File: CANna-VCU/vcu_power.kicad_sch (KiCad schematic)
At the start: 21 parts, among them U11 LMR33630CDDA, U12 LD1117S33TR_SOT223

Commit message: first draft of full board
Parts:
- added C21: 10uF, Capacitor_SMD:C_0402_1005Metric, symbol Device:C
- added D2: BZX84Cxx, Package_TO_SOT_SMD:SOT-23, symbol Diode:BZX84Cxx
- added Q1: FDN359BN, Package_TO_SOT_SMD:SOT-23_Handsoldering, symbol SUFST:FDN359BN
- added R9: 100k, Resistor_SMD:R_0402_1005Metric, symbol Device:R
- C20: renamed from C35; footprint Capacitor_SMD:C_0603_1608Metric -> Capacitor_SMD:C_0402_1005Metric
- C22: renamed from C36; footprint Capacitor_SMD:C_0603_1608Metric -> Capacitor_SMD:C_0402_1005Metric
- C23: renamed from C37; footprint Capacitor_SMD:C_0603_1608Metric -> Capacitor_SMD:C_0402_1005Metric
- C24: renamed from C38; footprint Capacitor_SMD:C_0603_1608Metric -> Capacitor_SMD:C_0402_1005Metric
- C25: renamed from C39; footprint Capacitor_SMD:C_0603_1608Metric -> Capacitor_SMD:C_0402_1005Metric
- C26: renamed from C40; footprint Capacitor_SMD:C_0603_1608Metric -> Capacitor_SMD:C_0402_1005Metric
- C27: renamed from C41; footprint Capacitor_SMD:C_0603_1608Metric -> Capacitor_SMD:C_0402_1005Metric
- C28: renamed from C42; footprint Capacitor_SMD:C_0603_1608Metric -> Capacitor_SMD:C_0402_1005Metric
- C29: renamed from C43; footprint Capacitor_SMD:C_0805_2012Metric_Pad1.18x1.45mm_HandSolder -> Capacitor_SMD:C_0402_1005Metric
- C30: renamed from C44; footprint Capacitor_SMD:C_0805_2012Metric_Pad1.18x1.45mm_HandSolder -> Capacitor_SMD:C_0402_1005Metric
- D3: renamed from D9; footprint (none) -> Diode_SMD:D_0603_1608Metric
- D4: renamed from D10; footprint (none) -> Diode_SMD:D_0603_1608Metric
- F1: renamed from F2; footprint (none) -> Fuse:Fuse_0603_1608Metric
- L1: footprint SR-Footprint-Library:XGL3520 -> Inductor_SMD:L_0603_1608Metric_Pad1.05x0.95mm_HandSolder
- R10: renamed from R82; footprint Resistor_SMD:R_0603_1608Metric -> Resistor_SMD:R_0402_1005Metric
- R11: renamed from R83; footprint Resistor_SMD:R_0603_1608Metric -> Resistor_SMD:R_0402_1005Metric
- R12: renamed from R84; footprint Resistor_SMD:R_0603_1608Metric -> Resistor_SMD:R_0402_1005Metric
- R13: renamed from R85; footprint Resistor_SMD:R_0805_2012Metric_Pad1.20x1.40mm_HandSolder -> Resistor_SMD:R_0402_1005Metric
- renumbered D11 to D5, U11 to U5, U12 to U6
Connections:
- net GND: now also C21.2, R9.1
- net +12V renamed +GLV_PROT
- net +GLV_PROT: now also C21.1, D2.3 (K), Q1.2 (S)
- net VBUS renamed +5V_UNPROT
- new net: D2.1 (A), Q1.1 (G), R9.2
- new net +GLV: Q1.3 (D)
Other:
- moved on the sheet: C20, C22, C23, C24, C29, C30, D3, D4, D5, F1, L1, R10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

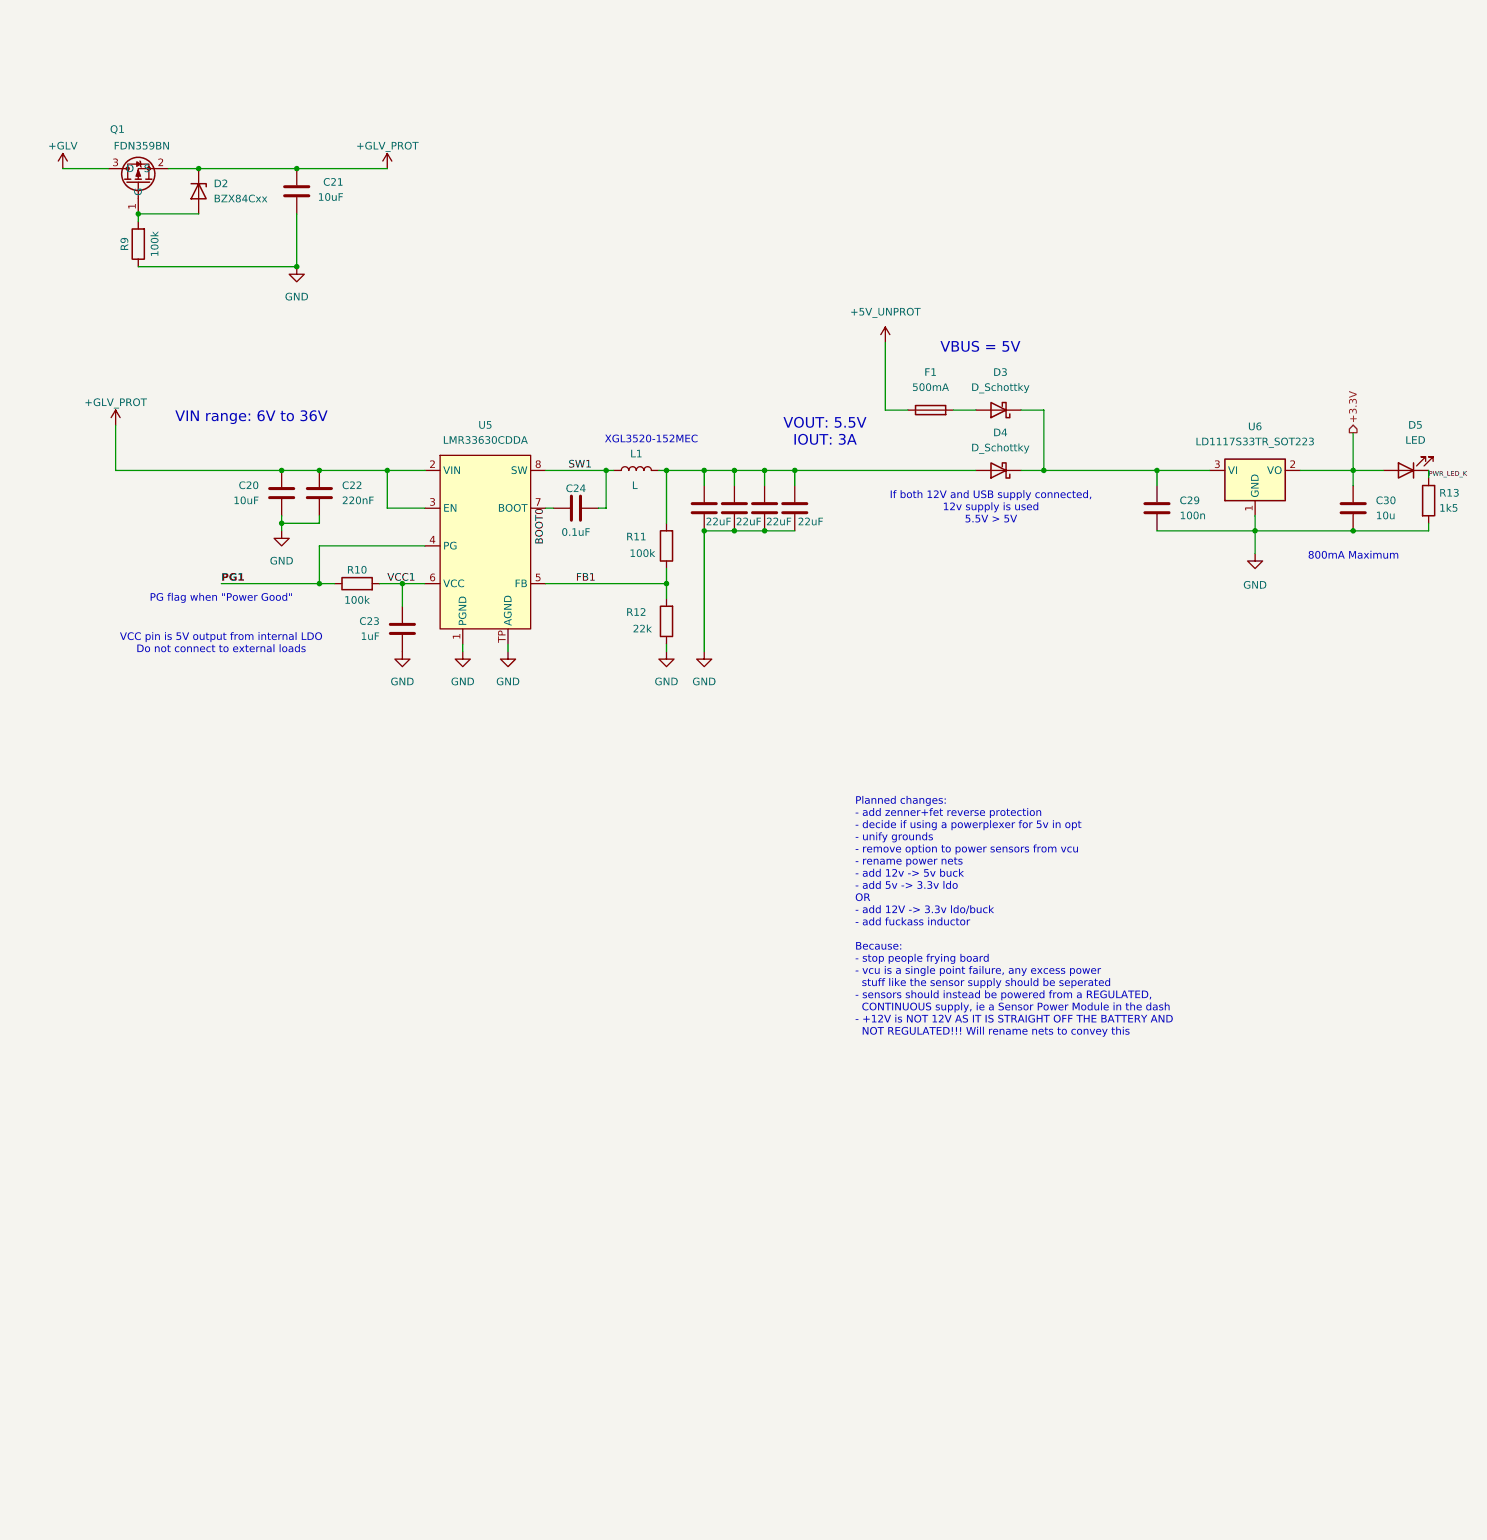
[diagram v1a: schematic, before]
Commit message: added power managment bits
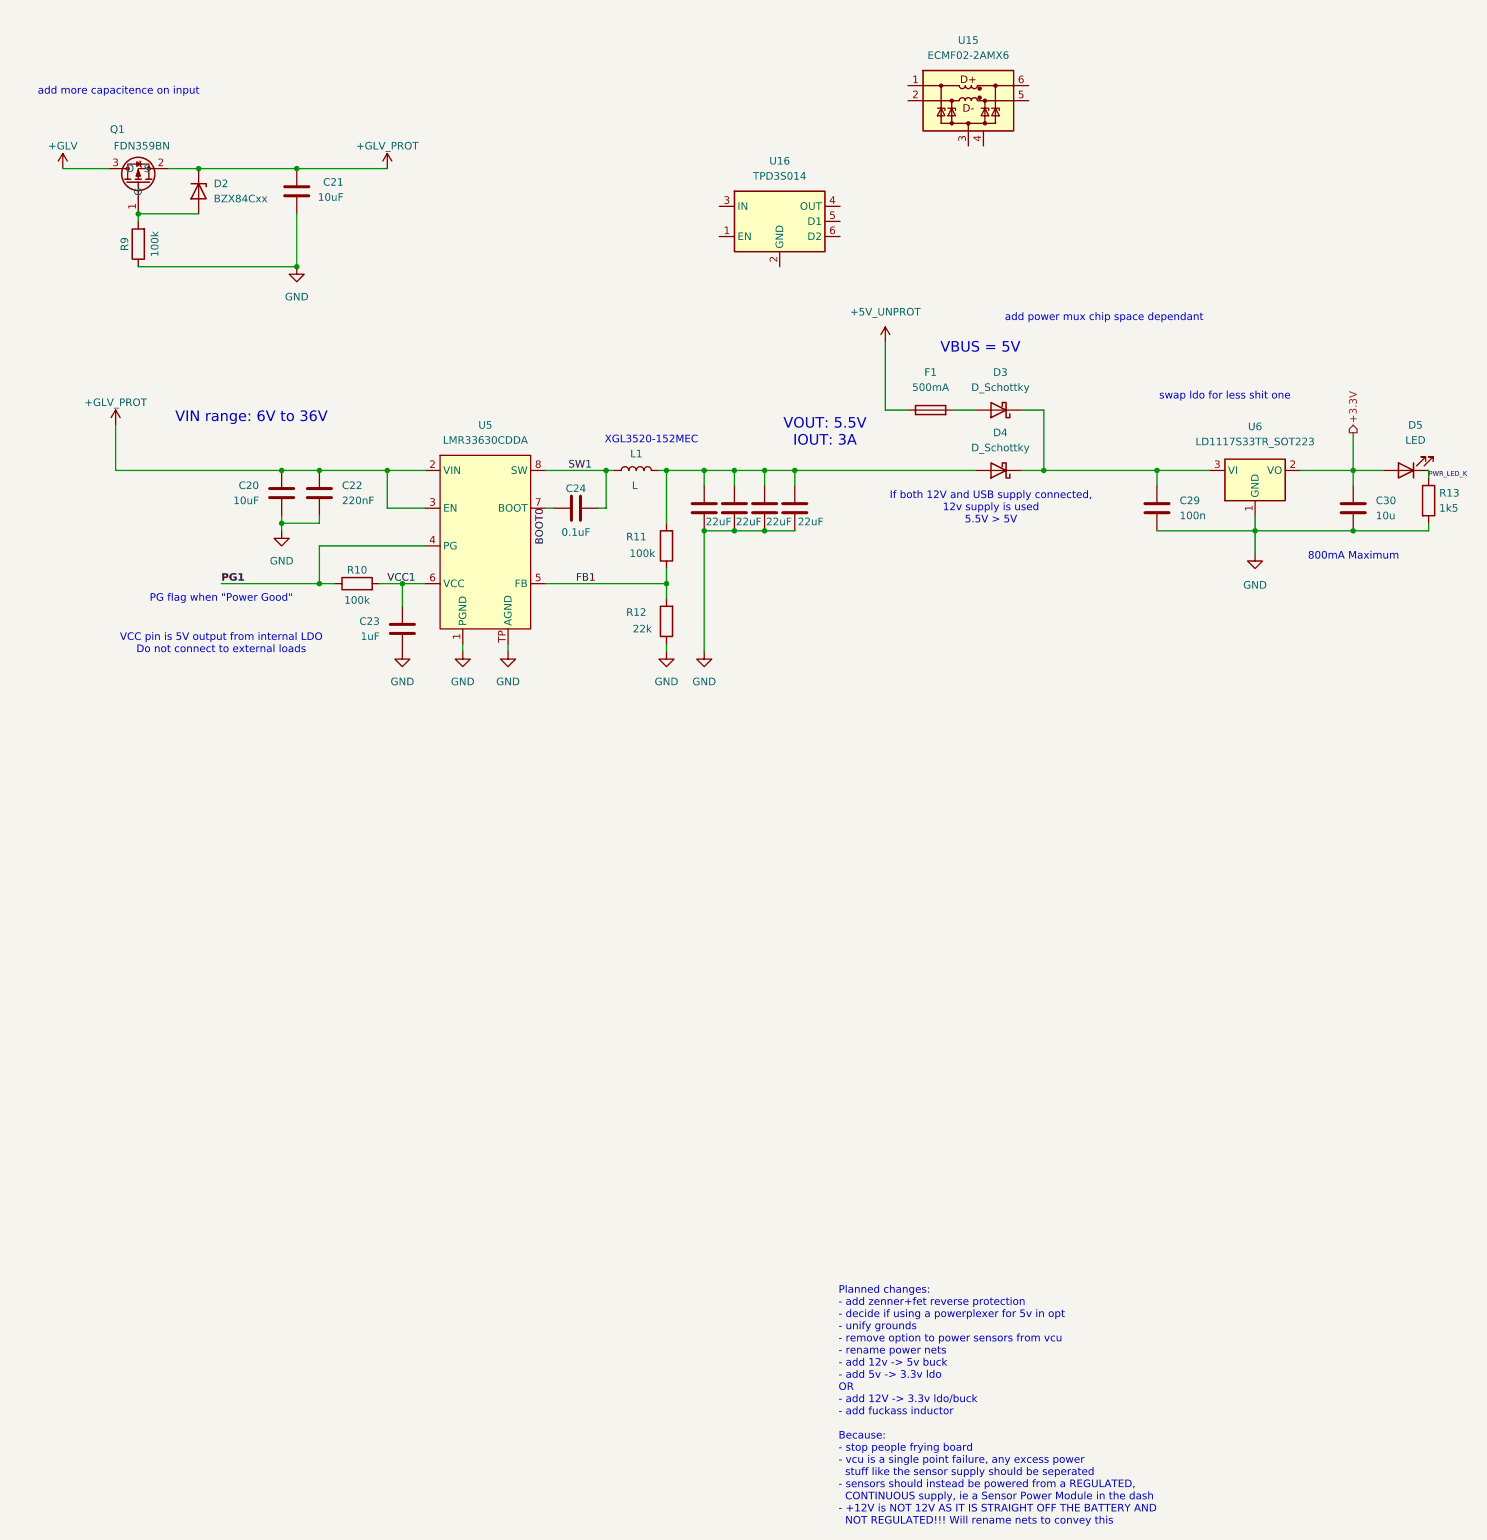
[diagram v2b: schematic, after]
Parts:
- added U15: ECMF02-2AMX6, Package_DFN_QFN:ST_UQFN-6L_1.5x1.7mm_P0.5mm, symbol Power_Protection:ECMF02-2AMX6
- added U16: TPD3S014, Package_TO_SOT_SMD:SOT-23-6, symbol Power_Protection:TPD3S014
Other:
- note added: "add more capacitence on input"
- note added: "add power mux chip space dependant"
- note added: "swap ldo for less shit one"
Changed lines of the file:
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@@
+		)
+	)
+	(text "add power mux chip space dependant"
+		(exclude_from_sim no)
+		(at 205.74 72.136 0)
+		(effects
+			(font
+				(size 1.27 1.27)
+			)
+		)
+	)
+	(text "swap ldo for less shit one"
+		(exclude_from_sim no)
+		(at 226.06 85.344 0)
+		(effects
+			(font
+				(size 1.27 1.27)
+			)
 		)
 	)
@@
 	(text "Planned changes:\n- add zenner+fet reverse protection \n- decide if using a powerplexer for 5v in opt\n- unify grounds\n- remove option to power sensors from vcu\n- rename power nets \n- add 12v -> 5v buck\n- add 5v -> 3.3v ldo\nOR\n- add 12V -> 3.3v ldo/buck\n- add fuckass inductor\n\nBecause:\n- stop people frying board\n- vcu is a single point failure, any excess power\n  stuff like the sensor supply should be seperated\n- sensors should instead be powered from a REGULATED,\n  CONTINUOUS supply, ie a Sensor Power Module in the dash\n- +12V is NOT 12V AS IT IS STRAIGHT OFF THE BATTERY AND \n  NOT REGULATED!!! Will rename nets to convey this"
 		(exclude_from_sim no)
-		(at 163.83 172.974 0)
+		(at 161.036 255.27 0)
 		(effects
 			(font
@@
 		)
 	)
+	(text "add more capacitence on input"
+		(exclude_from_sim no)
+		(at 39.878 34.036 0)
+		(effects
+			(font
+				(size 1.27 1.27)
+			)
+		)
+	)
 	(junction
 		(at 214.63 97.79)
@@
 	)
 	(image
-		(at 81.28 173.99)
+		(at 78.74 255.27)
 		(data "iVBORw0KGgoAAAANSUhEUgAAAjgAAADkCAIAAAAadMncAAAAA3NCSVQICAjb4U/gAAAACXBIWXMA"
 			"ABJcAAASXAFoxDaJAAAgAElEQVR4nO3deVxU9f4/8Pcs7AMMmxLrKKTkxuCK+1hplpl4NeTnBui1"
@@
 	)
 	(symbol
+		(lib_id "Power_Protection:TPD3S014")
+		(at 151.13 55.88 0)
+		(unit 1)
+		(exclude_from_sim no)
+		(in_bom yes)
+		(on_board yes)
+		(dnp no)
+		(fields_autoplaced yes)
+		(property "Reference" "U16"
+			(at 151.13 45.72 0)
+			(effects
+				(font
+					(size 1.27 1.27)
+				)
+			)
+		)
+		(property "Value" "TPD3S014"
+			(at 151.13 48.26 0)
+			(effects
+				(font
+					(size 1.27 1.27)
+				)
+			)
+		)
+		(property "Footprint" "Package_TO_SOT_SMD:SOT-23-6"
+			(at 151.13 46.99 0)
+			(effects
+				(font
+					(size 1.27 1.27)
+				)
+				(hide yes)
+			)
+		)
+		(property "Datasheet" "http://www.ti.com/lit/ds/symlink/tpd3s014.pdf"
+			(at 146.05 49.53 0)
+			(effects
+				(font
+					(size 1.27 1.27)
+				)
+				(hide yes)
+			)
+		)
+		(property "Description" "Current Limit Switch and D+/D– ESD Protection for USB Host Port, 0.5A, SOT-23-6"
+			(at 151.13 55.88 0)
+			(effects
+				(font
+					(size 1.27 1.27)
+				)
+				(hide yes)
+			)
+		)
+		(pin "2"
+		)
+		(pin "5"
+		)
+		(pin "4"
+		)
+		(pin "3"
+		)
+		(pin "6"
+		)
+		(pin "1"
+		)
+		(instances
+			(project ""
+				(path "/d2b041cf-e68d-49d7-b31d-fe6ebce83d7e/33c87969-d543-4809-83eb-5f9a35fc6ce2"
+					(reference "U16")
+					(unit 1)
+				)
+			)
+		)
+	)
+	(symbol
 		(lib_id "Device:R")
 		(at 80.01 116.84 90)
@@
 					(unit 1)
 				)
+			)
+		)
+	)
+	(symbol
+		(lib_id "Power_Protection:ECMF02-2AMX6")
+		(at 182.88 35.56 0)
+		(unit 1)
+		(exclude_from_sim no)
+		(in_bom yes)
+		(on_board yes)
+		(dnp no)
+		(fields_autoplaced yes)
+		(property "Reference" "U15"
+			(at 182.88 25.4 0)
+			(effects
+				(font
+					(size 1.27 1.27)
+				)
+			)
+		)
+		(property "Value" "ECMF02-2AMX6"
+			(at 182.88 27.94 0)
+			(effects
+				(font
+					(size 1.27 1.27)
+				)
+			)
+		)
+		(property "Footprint" "Package_DFN_QFN:ST_UQFN-6L_1.5x1.7mm_P0.5mm"
+			(at 182.88 55.88 0)
+			(effects
+				(font
+					(size 1.27 1.27)
+				)
+				(hide yes)
+			)
+		)
+		(property "Datasheet" "https://www.st.com/resource/en/datasheet/ecmf02-2amx6.pdf"
+			(at 182.88 58.42 0)
+			(effects
+				(font
+					(size 1.27 1.27)
+				)
+				(hide yes)
+			)
+		)
+		(property "Description" "Single Pair Common Mode Filter with ESD Protection, UQFN-6L"
+			(at 182.88 35.56 0)
+			(effects
+				(font
+					(size 1.27 1.27)
+				)
+				(hide yes)
+			)
+		)
+		(pin "2"
+		)
+		(pin "1"
+		)
+		(pin "3"
+		)
+		(pin "4"
+		)
+		(pin "6"
+		)
+		(pin "5"
+		)
+		(instances
+			(project ""
+				(path "/d2b041cf-e68d-49d7-b31d-fe6ebce83d7e/33c87969-d543-4809-83eb-5f9a35fc6ce2"
+					(reference "U15")
+					(unit 1)
+				)
